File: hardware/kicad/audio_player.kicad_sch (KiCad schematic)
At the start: 19 parts, among them J1 AudioJack3_Switch, J2 Conn_01x06_Pin, SW1 SW_Push, SW2 RotaryEncoder_Switch, U1 IP5306-I2C, U2 PCM5102A, U3 TPA6132A2RTE, U4 AP2112K-3.3

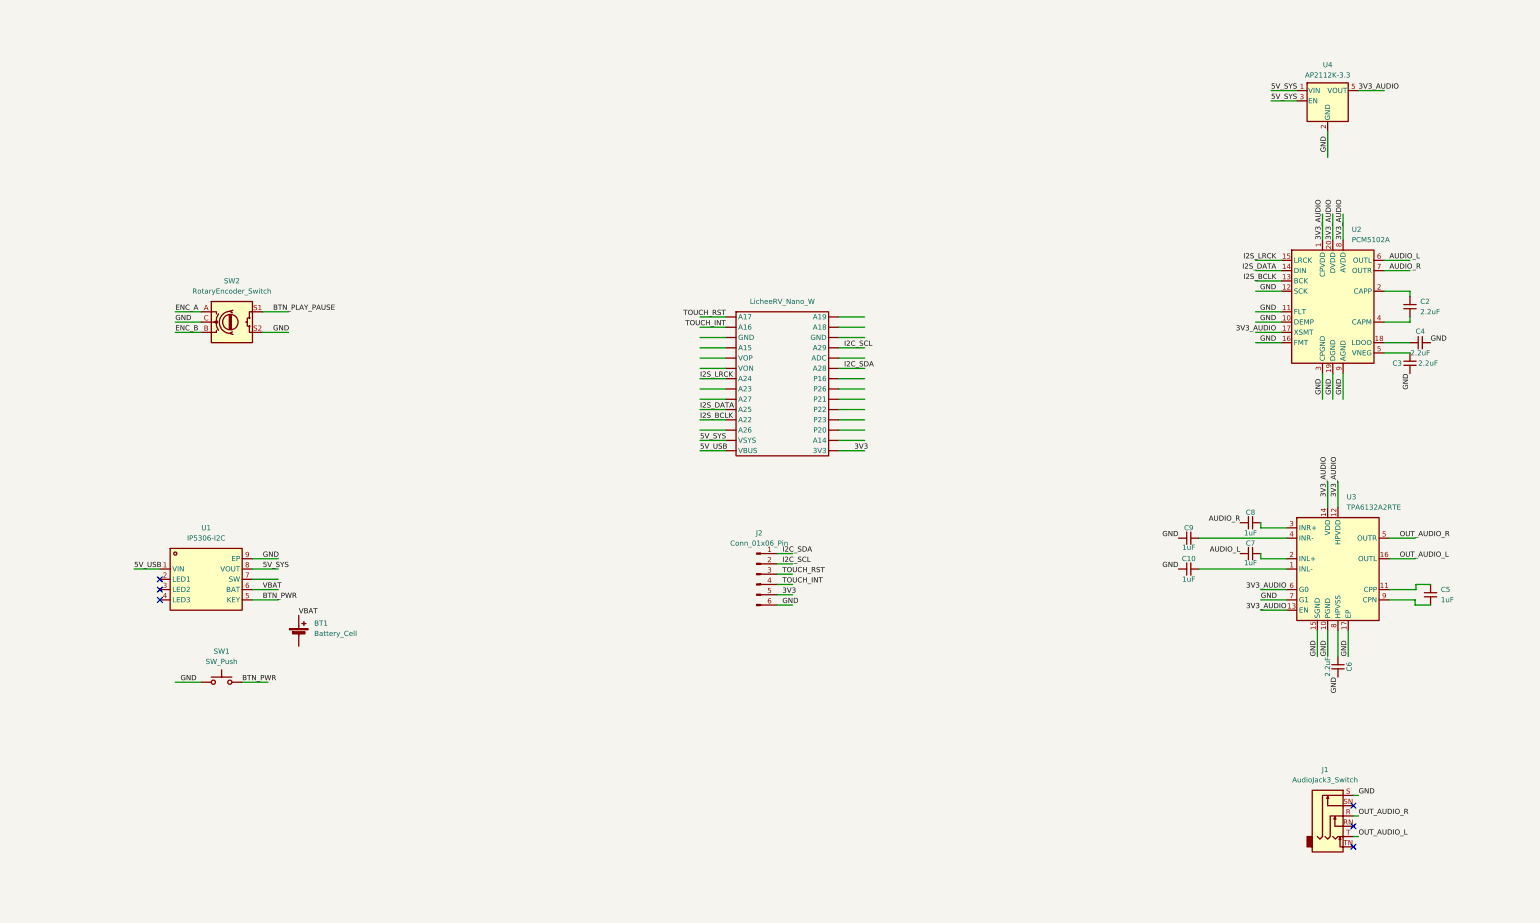
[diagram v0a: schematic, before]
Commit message: hardware: update symb of licheerv(from official site) and delete extra wires so make sch prettier
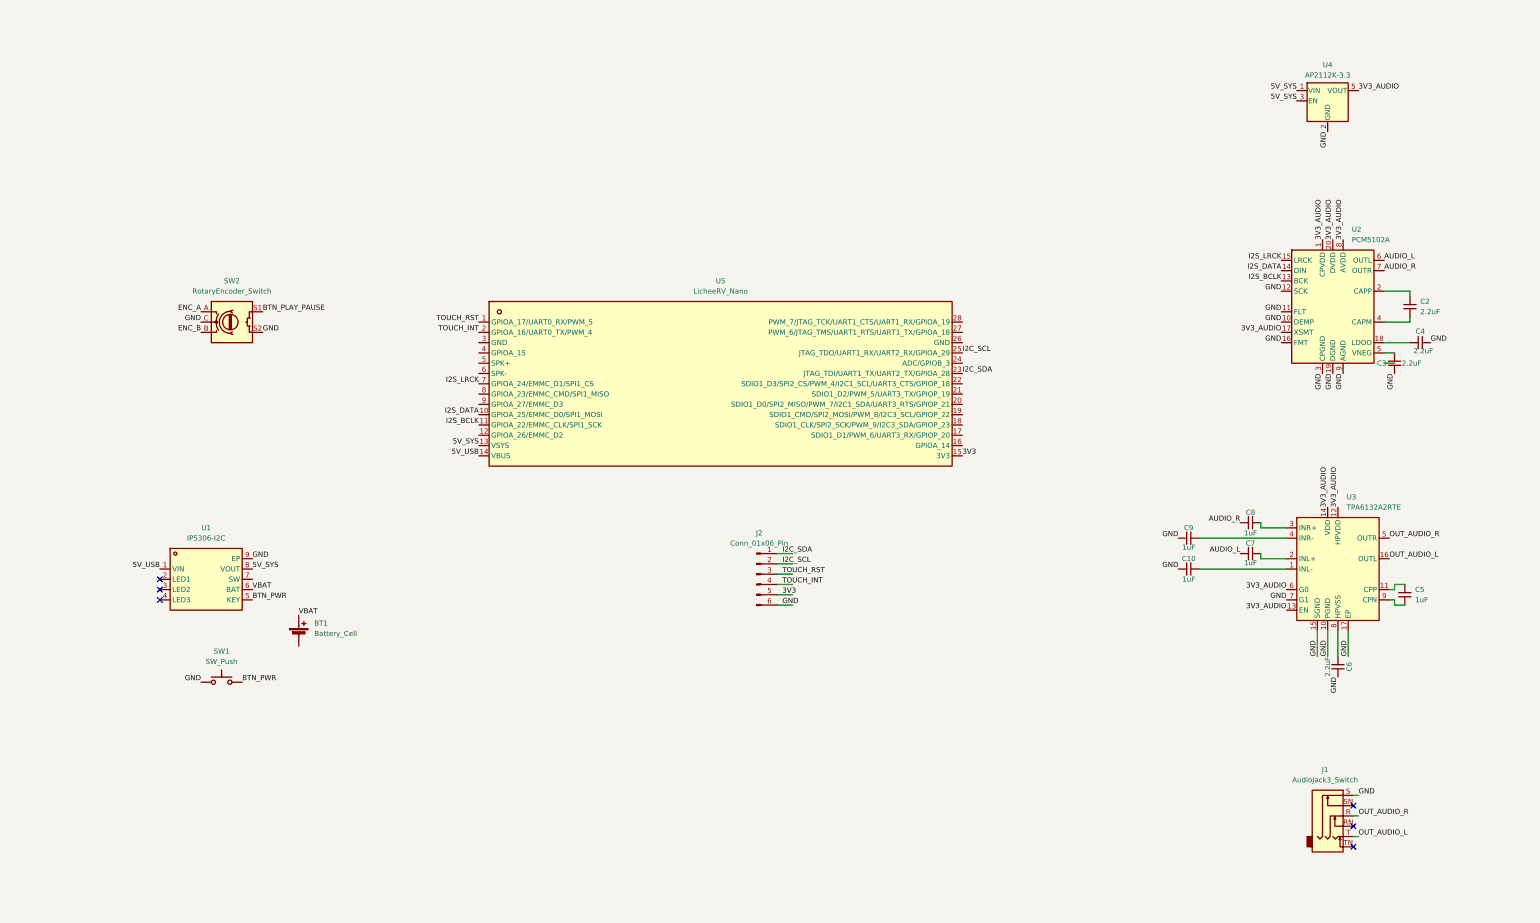
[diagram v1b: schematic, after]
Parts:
- removed LicheeRV_Nano_W: (no value), symbol licheeRV_Nano_W_Library:LicheeRV_Nano_W
- added U5: LicheeRV_Nano, Module:LicheeRV_Nano, symbol licheerv_nano_w:LicheeRV_Nano
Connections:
- net 3V3: now also U5.15 (3V3)
- net 5V_SYS: now also U5.13 (VSYS)
- net 5V_USB: now also U5.14 (VBUS)
- net I2C_SCL: now also U5.25 (JTAG_TDO/UART1_RX/UART2_RX/GPIOA_29)
- net I2C_SDA: now also U5.23 (JTAG_TDI/UART1_TX/UART2_TX/GPIOA_28)
- net I2S_BCLK: now also U5.11 (GPIOA_22/EMMC_CLK/SPI1_SCK)
- net I2S_DATA: now also U5.10 (GPIOA_25/EMMC_D0/SPI1_MOSI)
- net I2S_LRCK: now also U5.7 (GPIOA_24/EMMC_D1/SPI1_CS)
- net TOUCH_INT: now also U5.2 (GPIOA_16/UART0_TX/PWM_4)
- net TOUCH_RST: now also U5.1 (GPIOA_17/UART0_RX/PWM_5)
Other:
- moved on the sheet: C3, C5

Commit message: docs: init hardware docs file
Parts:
- removed U4: AP2112K-3.3, Package_TO_SOT_SMD:SOT-23-5, symbol Regulator_Linear:AP2112K-3.3
- added IC1: XC6220B331PR-G, XC6220B331PRG, symbol XC6220B331PR-G:XC6220B331PR-G
- added U6: INA219AxD, Package_SO:SOIC-8_3.9x4.9mm_P1.27mm, symbol Sensor_Energy:INA219AxD
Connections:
- net GND: now also IC1.2 (VSS)
- no-connect marks 6 -> 3
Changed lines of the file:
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@@
-	)
-	(no_connect
-		(at 66.04 166.37)
 	)
 	(no_connect
@@
 	)
 	(no_connect
-		(at 66.04 171.45)
-	)
-	(no_connect
 		(at 360.68 222.25)
 	)
-	(no_connect
-		(at 66.04 168.91)
-	)
 	(wire
 		(pts
@@
 		(pts
 			(xy 354.33 185.42) (xy 354.33 179.07)
-		)
-		(stroke
-			(width 0)
-			(type default)
-		)
-	)
-	(wire
-		(pts
-			(xy 368.3 113.03) (xy 370.84 113.03)
 		)
 		(stroke
@@
 	)
 	(label "GND"
-		(at 354.33 55.88 270)
+		(at 341.63 46.99 180)
 		(effects
 			(font
@@
 	)
 	(label "5V_SYS"
-		(at 346.71 48.26 180)
+		(at 335.28 52.07 180)
 		(effects
 			(font
@@
 	)
 	(label "3V3_AUDIO"
-		(at 361.95 45.72 0)
+		(at 373.38 44.45 0)
 		(effects
 			(font
@@
 	)
 	(label "5V_SYS"
-		(at 346.71 45.72 180)
+		(at 335.28 44.45 180)
 		(effects
 			(font
@@
 	)
 	(symbol
-		(lib_id "Regulator_Linear:AP2112K-3.3")
-		(at 354.33 48.26 0)
-		(unit 1)
-		(body_style 1)
-		(exclude_from_sim no)
-		(in_bom yes)
-		(on_board yes)
-		(in_pos_files yes)
-		(dnp no)
-		(fields_autoplaced yes)
-		(property "Reference" "U4"
-			(at 354.33 39.37 0)
-			(show_name no)
-			(do_not_autoplace no)
-			(effects
-				(font
-					(size 1.27 1.27)
-				)
-			)
-		)
-		(property "Value" "AP2112K-3.3"
-			(at 354.33 41.91 0)
-			(show_name no)
-			(do_not_autoplace no)
-			(effects
-				(font
-					(size 1.27 1.27)
-				)
-			)
-		)
-		(property "Footprint" "Package_TO_SOT_SMD:SOT-23-5"
-			(at 354.33 40.005 0)
-			(hide yes)
-			(show_name no)
-			(do_not_autoplace no)
-			(effects
-				(font
-					(size 1.27 1.27)
-				)
-			)
-		)
-		(property "Datasheet" "https://www.diodes.com/assets/Datasheets/AP2112.pdf"
-			(at 354.33 45.72 0)
-			(hide yes)
-			(show_name no)
-			(do_not_autoplace no)
-			(effects
-				(font
-					(size 1.27 1.27)
-				)
-			)
-		)
-		(property "Description" "600mA low dropout linear regulator, with enable pin, 3.8V-6V input voltage range, 3.3V fixed positive output, SOT-23-5"
-			(at 354.33 48.26 0)
-			(hide yes)
-			(show_name no)
-			(do_not_autoplace no)
-			(effects
-				(font
-					(size 1.27 1.27)
-				)
-			)
-		)
-		(pin "3"
-		)
-		(pin "5"
-		)
-		(pin "2"
-		)
-		(pin "4"
-		)
-		(pin "1"
-		)
-		(instances
-			(project "audio_player"
-				(path "/b494b84f-4846-40ac-b373-a226c6c544f1"
-					(reference "U4")
-					(unit 1)
-				)
-			)
-		)
-	)
-	(symbol
 		(lib_id "Device:C_Small")
 		(at 356.87 187.96 0)
@@
 	)
 	(symbol
+		(lib_id "Sensor_Energy:INA219AxD")
+		(at 43.18 171.45 0)
+		(unit 1)
+		(body_style 1)
+		(exclude_from_sim no)
+		(in_bom yes)
+		(on_board yes)
+		(in_pos_files yes)
+		(dnp no)
+		(fields_autoplaced yes)
+		(property "Reference" "U6"
+			(at 45.3233 158.75 0)
+			(show_name no)
+			(do_not_autoplace no)
+			(effects
+				(font
+					(size 1.27 1.27)
+				)
+				(justify left)
+			)
+		)
+		(property "Value" "INA219AxD"
+			(at 45.3233 161.29 0)
+			(show_name no)
+			(do_not_autoplace no)
+			(effects
+				(font
+					(size 1.27 1.27)
+				)
+				(justify left)
+			)
+		)
+		(property "Footprint" "Package_SO:SOIC-8_3.9x4.9mm_P1.27mm"
+			(at 63.5 180.34 0)
+			(hide yes)
+			(show_name no)
+			(do_not_autoplace no)
+			(effects
+				(font
+					(size 1.27 1.27)
+				)
+			)
+		)
+		(property "Datasheet" "http://www.ti.com/lit/ds/symlink/ina219.pdf"
+			(at 52.07 173.99 0)
+			(hide yes)
+			(show_name no)
+			(do_not_autoplace no)
+			(effects
+				(font
+					(size 1.27 1.27)
+				)
+			)
+		)
+		(property "Description" "Zero-Drift, Bidirectional Current/Power Monitor (0-26V) With I2C Interface, SOIC-8"
+			(at 43.18 171.45 0)
+			(hide yes)
+			(show_name no)
+			(do_not_autoplace no)
+			(effects
+				(font
+					(size 1.27 1.27)
+				)
+			)
+		)
+		(pin "6"
+		)
+		(pin "8"
+		)
+		(pin "7"
+		)
+		(pin "4"
+		)
+		(pin "5"
+		)
+		(pin "3"
+		)
+		(pin "1"
+		)
+		(pin "2"
+		)
+		(instances
+			(project "audio_player"
+				(path "/b494b84f-4846-40ac-b373-a226c6c544f1"
+					(reference "U6")
+					(unit 1)
+				)
+			)
+		)
+	)
+	(symbol
 		(lib_id "Device:C_Small")
 		(at 335.28 152.4 90)
@@
 					(unit 1)
 				)
+			)
+		)
+	)
+	(symbol
+		(lib_id "XC6220B331PR-G:XC6220B331PR-G")
+		(at 341.63 44.45 0)
+		(unit 1)
+		(body_style 1)
+		(exclude_from_sim no)
+		(in_bom yes)
+		(on_board yes)
+		(in_pos_files yes)
+		(dnp no)
+		(fields_autoplaced yes)
+		(property "Reference" "IC1"
+			(at 355.6 36.83 0)
+			(show_name no)
+			(do_not_autoplace no)
+			(effects
+				(font
+					(size 1.27 1.27)
+				)
+			)
+		)
+		(property "Value" "XC6220B331PR-G"
+			(at 355.6 39.37 0)
+			(show_name no)
+			(do_not_autoplace no)
+			(effects
+				(font
+					(size 1.27 1.27)
+				)
+			)
+		)
+		(property "Footprint" "XC6220B331PRG"
+			(at 365.76 139.37 0)
+			(hide yes)
+			(show_name no)
+			(do_not_autoplace no)
+			(effects
+				(font
+					(size 1.27 1.27)
+				)
+				(justify left top)
+			)
+		)
+		(property "Datasheet" "https://www.digikey.ph/en/products/detail/torex-semiconductor-ltd/XC6220B331PR-G/2138172"
+			(at 365.76 239.37 0)
+			(hide yes)
+			(show_name no)
+			(do_not_autoplace no)
+			(effects
+				(font
+					(size 1.27 1.27)
+				)
+				(justify left top)
+			)
+		)
+		(property "Description" "Linear Voltage Regulator IC Positive Fixed 1 Output 1A SOT-89-5"
+			(at 341.63 44.45 0)
+			(hide yes)
+			(show_name no)
+			(do_not_autoplace no)
+			(effects
+				(font
+					(size 1.27 1.27)
+				)
+			)
+		)
+		(property "Height" "1.6"
+			(at 365.76 439.37 0)
+			(hide yes)
+			(show_name no)
+			(do_not_autoplace no)
+			(effects
+				(font
+					(size 1.27 1.27)
+				)
+				(justify left top)
+			)
+		)
+		(property "Manufacturer_Name" "Torex"
+			(at 365.76 539.37 0)
+			(hide yes)
+			(show_name no)
+			(do_not_autoplace no)
+			(effects
+				(font
+					(size 1.27 1.27)
+				)
+				(justify left top)
+			)
+		)
+		(property "Manufacturer_Part_Number" "XC6220B331PR-G"
+			(at 365.76 639.37 0)
+			(hide yes)
+			(show_name no)
+			(do_not_autoplace no)
+			(effects
+				(font
+					(size 1.27 1.27)
+				)
+				(justify left top)
+			)
+		)
+		(property "Mouser Part Number" "865-XC6220B331PR-G"
+			(at 365.76 739.37 0)
+			(hide yes)
+			(show_name no)
+			(do_not_autoplace no)
+			(effects
+				(font
+					(size 1.27 1.27)
+				)
+				(justify left top)
+			)
+		)
+		(property "Mouser Price/Stock" "https://www.mouser.co.uk/ProductDetail/Torex-Semiconductor/XC6220B331PR-G?qs=AsjdqWjXhJ9%2FMkHVs5v3gw%3D%3D"
+			(at 365.76 839.37 0)
+			(hide yes)
+			(show_name no)
+			(do_not_autoplace no)
+			(effects
+				(font
+					(size 1.27 1.27)
+				)
+				(justify left top)
+			)
+		)
+		(property "Arrow Part Number" ""
+			(at 365.76 939.37 0)
+			(hide yes)
+			(show_name no)
+			(do_not_autoplace no)
+			(effects
+				(font
+					(size 1.27 1.27)
+				)
+				(justify left top)
+			)
+		)
+		(property "Arrow Price/Stock" ""
+			(at 365.76 1039.37 0)
+			(hide yes)
+			(show_name no)
+			(do_not_autoplace no)
+			(effects
+				(font
+					(size 1.27 1.27)
+				)
+				(justify left top)
+			)
+		)
+		(pin "6"
+		)
+		(pin "5"
+		)
+		(pin "1"
+		)
+		(pin "7"
+		)
+		(pin "2"
+		)
+		(pin "4"
+		)
+		(pin "3"
+		)
+		(instances
+			(project "audio_player"
+				(path "/b494b84f-4846-40ac-b373-a226c6c544f1"
+					(reference "IC1")
+					(unit 1)
+				)

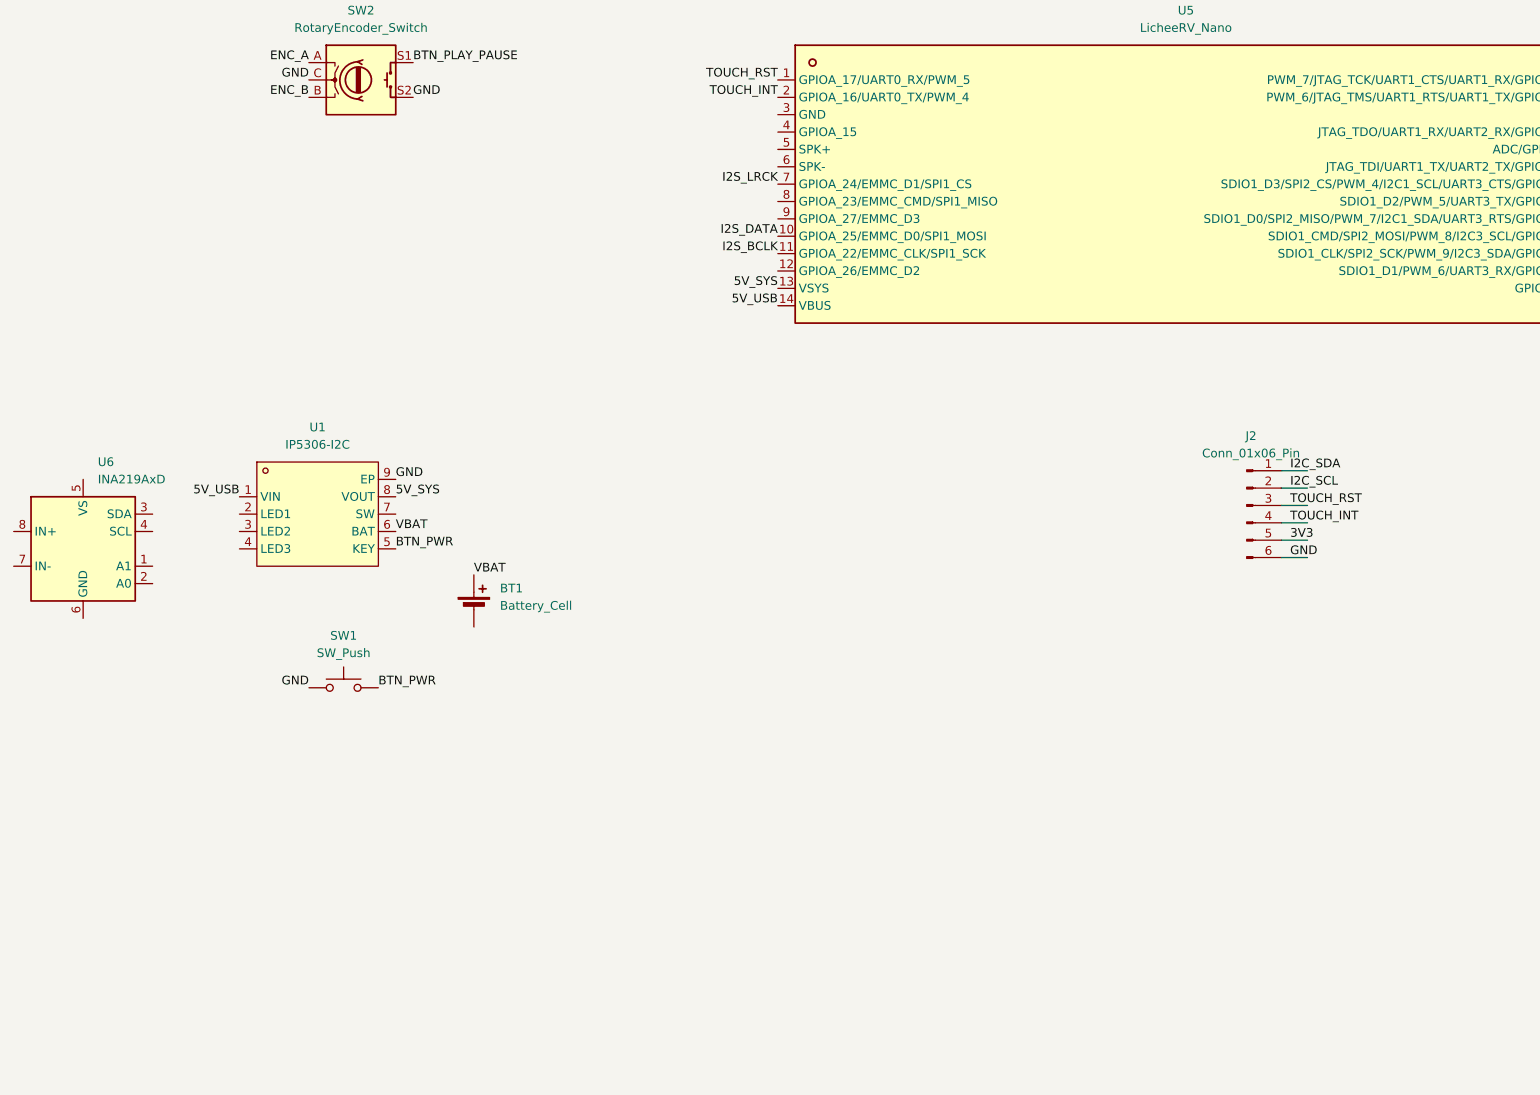
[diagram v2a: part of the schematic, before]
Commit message: kicad_sch: add IP5306 peripheral elements
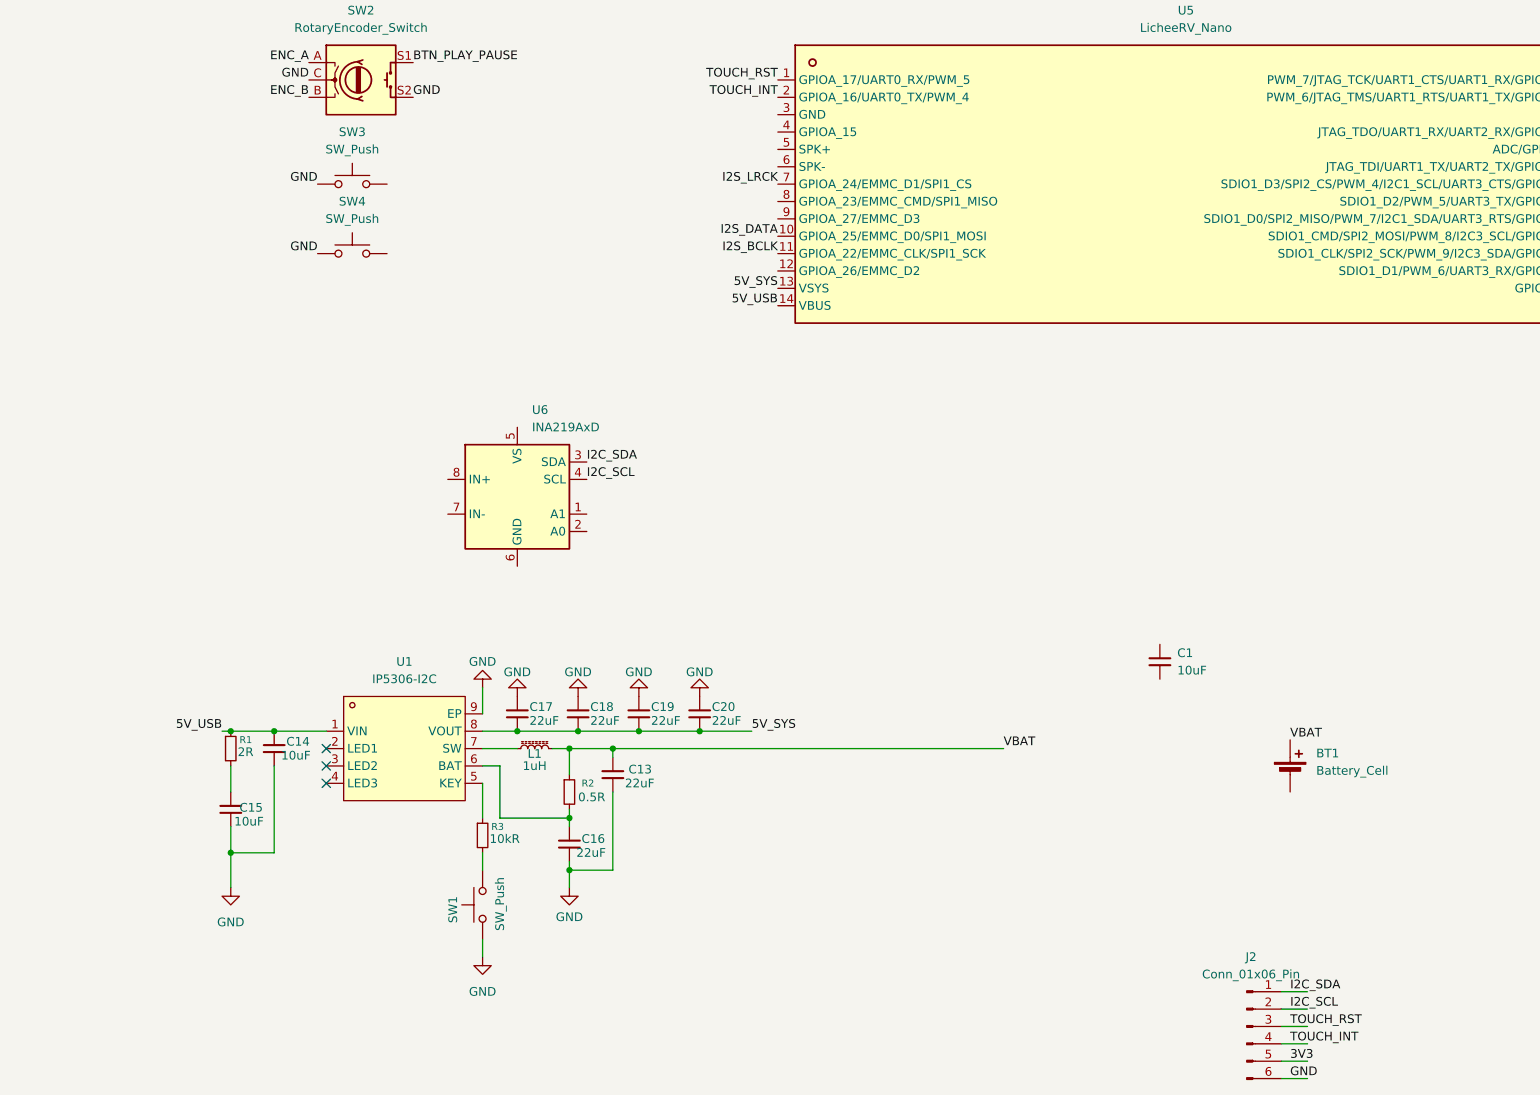
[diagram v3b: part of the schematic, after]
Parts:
- added C1, C14, C15: 10uF, symbol Device:C_Small
- added C13, C16, C17, C18, C19, C20: 22uF, symbol Device:C_Small
- added L1: 1uH, symbol Device:L_Ferrite_Small
- added R1: 2R, symbol Device:R_Small
- added R2: 0.5R, symbol Device:R_Small
- added R3: 10kR, symbol Device:R_Small
- added SW3, SW4: SW_Push, symbol Switch:SW_Push
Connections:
- net 5V_SYS: now also C17.2, C18.2, C19.2, C20.2
- net 5V_USB: now also C14.1, R1.1
- net GND: now also C13.2, C14.2, C15.2, C16.2, C17.1, C18.1, C19.1, C20.1, SW3.1, SW4.1
- net I2C_SCL: now also U6.4 (SCL)
- net I2C_SDA: now also U6.3 (SDA)
- net VBAT: now also C13.1, L1.2, R2.1; no longer U1.6 (BAT)
- net at U1.7 (SW): now also L1.1
- net BTN_PWR: no longer names the net of SW1.2
- net BTN_PWR: now also R3.2; no longer U1.5 (KEY)
- new net: C16.1, R2.2, U1.6 (BAT)
- new net: R3.1, U1.5 (KEY)
- new net: C15.1, R1.2
- no-connect marks 3 -> 6
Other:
- moved on the sheet: BT1, J2, SW1, U1, U6
